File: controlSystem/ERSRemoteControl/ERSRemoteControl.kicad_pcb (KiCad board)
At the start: 2 copper layers, 58.8 x 37.7 mm, 58 parts, among them J1 USB_C_Receptacle_USB2.0_14P, J2 0022-232041, J5 0022-232021, J6 0022-232021, J7 0022-232031, SW2 SW_Push, SW3 SW_Push, SW4 SW_Push, SW5 SW_Push, SW6 SW_Push, SW7 SW_Push, U1 TPS63070, U2 ESP32-S3-WROOM-1

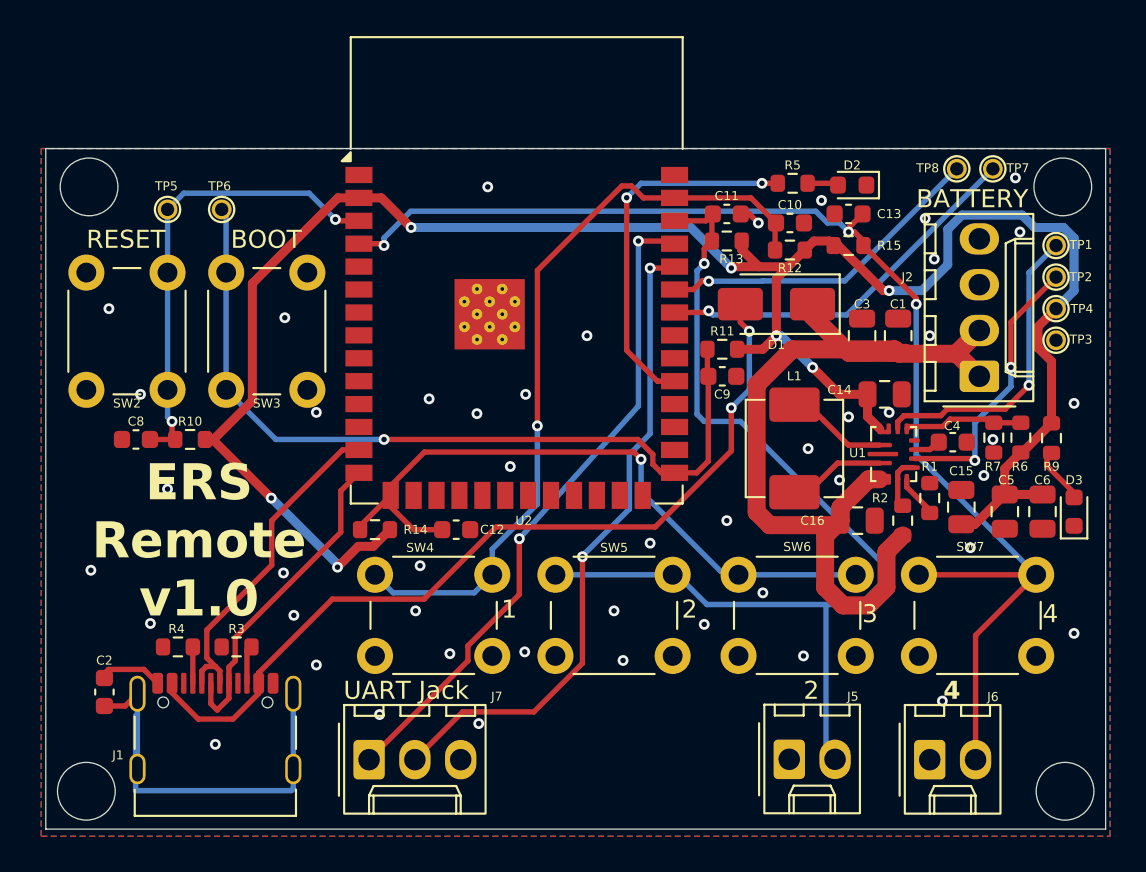
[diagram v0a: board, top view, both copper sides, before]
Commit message: Design review, set board constraints to osh park two layer, fix library paths, etc
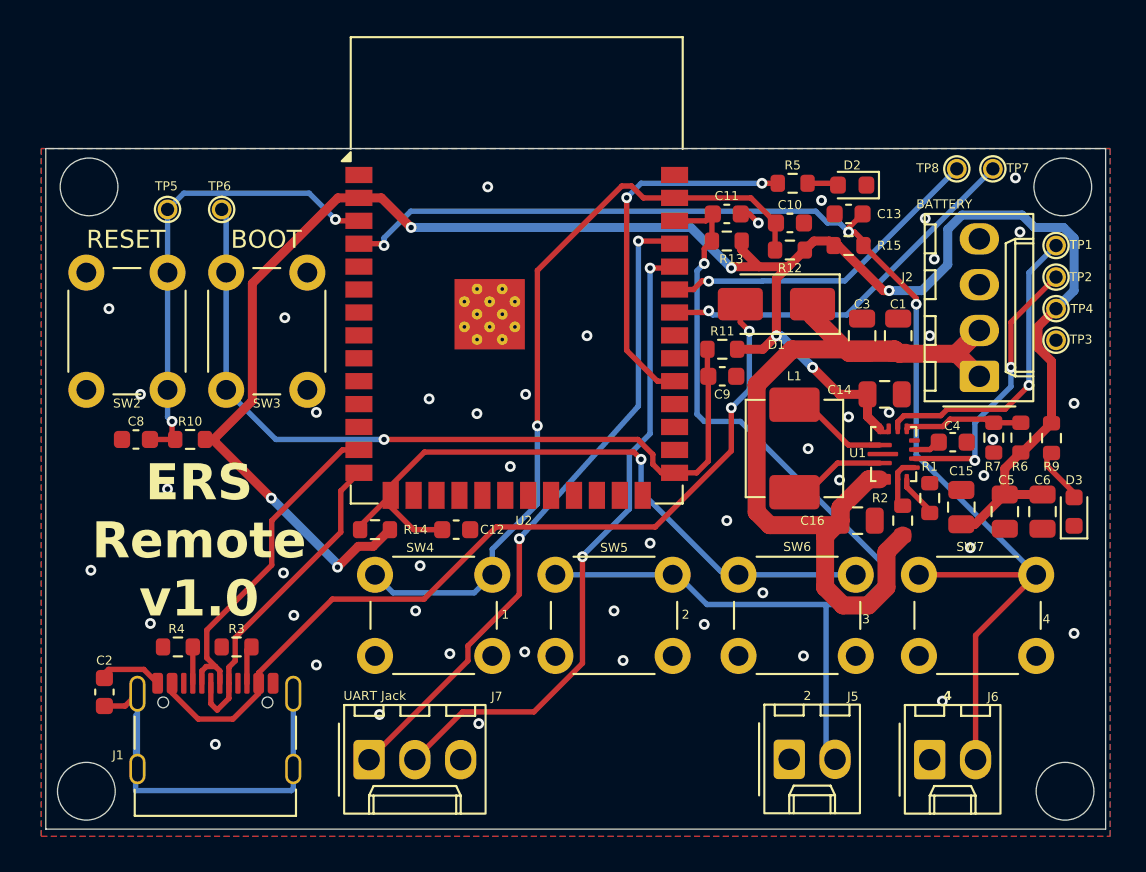
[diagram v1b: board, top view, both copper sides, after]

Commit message: Fixed library issues and completed design review changes
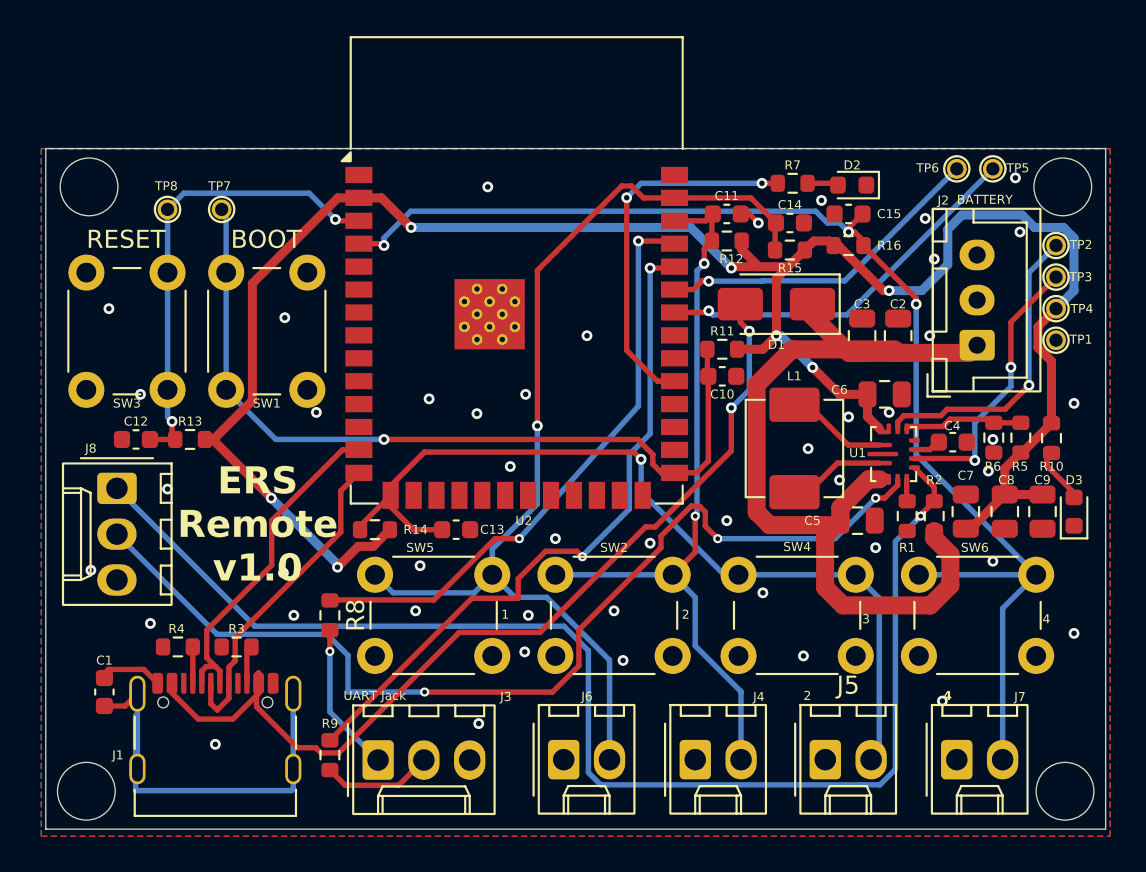
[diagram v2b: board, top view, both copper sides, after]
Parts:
- added J5: 0022-232021, Connector_Molex:Molex_KK-254_AE-6410-02A_1x02_P2.54mm_Vertical, F.Cu at (117.2, 124.8)
- added J6: 0022-232021, Connector_Molex:Molex_KK-254_AE-6410-02A_1x02_P2.54mm_Vertical, F.Cu at (102.7, 124.8)
- added J8: 0022-232031, Connector_Molex:Molex_KK-254_AE-6410-03A_1x03_P2.54mm_Vertical, F.Cu at (77.9, 109.7)
- added R8: 100, Resistor_SMD:R_0603_1608Metric, F.Cu at (89.8, 116.8)
- added R9: 100, Resistor_SMD:R_0603_1608Metric, F.Cu at (89.8, 124.5)
- J2: value 0022-232041 -> B3B-XH-A; footprint Connector_Molex:Molex_KK-254_AE-6410-04A_1x04_P2.54mm_Vertical -> Connector_JST:JST_XH_B3B-XH-A_1x03_P2.50mm_Vertical
- moved J4 5.21 mm to (110.0, 124.8)
- moved R2 1.77 mm to (123.2, 111.2), turned to -90 degrees
- moved J2 1.73 mm to (125.6, 101.8)
- moved R1 1.60 mm to (121.8, 111.2), turned to -90 degrees
- moved J7 1.50 mm to (124.5, 124.8)
- moved J3 0.50 mm to (92.4, 124.8)
- moved C7 0.35 mm to (125.0, 111.0)
- renumbered C2 to C1, C9 to C10, C8 to C12, C12 to C13, C10 to C14, C13 to C15, C1 to C2, C16 to C5, C14 to C6, C15 to C7, C5 to C8, C6 to C9, J7 to J3, J5 to J4, J6 to J7, R9 to R10, R13 to R12, R10 to R13, R12 to R15, R15 to R16, R6 to R5, R7 to R6, R5 to R7, SW3 to SW1, SW5 to SW2, SW2 to SW3, SW6 to SW4, SW4 to SW5, SW7 to SW6, TP3 to TP1, TP1 to TP2, TP2 to TP3, TP7 to TP5, TP8 to TP6, TP6 to TP7, TP5 to TP8
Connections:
- J2 pad 2: Net-(D1-K) -> unconnected-(J2-Pin_2-Pad2)
- J3 pad 1: Net-(J7-Pin_1) -> Net-(J3-Pin_1)
- J3 pad 2: Net-(J7-Pin_2) -> Net-(J3-Pin_2)
- R2 pad 1: Net-(D1-K) -> Net-(J8-Pin_1)
- R2 pad 2: Net-(U1-EN) -> Net-(D1-K)
- U1 pad 1: Net-(U1-EN) -> Net-(J8-Pin_1)
- U1 pad 14: Net-(U1-EN) -> Net-(J8-Pin_2)
- U2 pad 36: Net-(J7-Pin_2) -> Net-(U2-RXD0)
- U2 pad 37: Net-(J7-Pin_1) -> Net-(U2-TXD0)
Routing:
- net Net-(J8-Pin_1): track 0.00 -> 72.3 mm, vias 0 -> 1
- net Net-(J8-Pin_2): track 0.00 -> 56.7 mm, vias 0 -> 3
- net Net-(U2-RXD0): track 0.00 -> 38.0 mm, vias 0 -> 2
- net Net-(J7-Pin_1): track 36.8 -> 0.00 mm, vias 2 -> 0
- net Net-(J7-Pin_2): track 36.4 -> 0.00 mm, vias 2 -> 0
- net Net-(U2-TXD0): track 0.00 -> 33.0 mm, vias 0 -> 2
- net /SWITCH 2: track 56.9 -> 41.8 mm, vias 1 -> 2
- net /SWITCH 1: track 42.8 -> 56.7 mm
- net /SWITCH 3: track 37.6 -> 48.5 mm
- net Net-(J3-Pin_1): track 0.00 -> 8.30 mm, vias 0 -> 1
- net Net-(J3-Pin_2): track 0.00 -> 6.14 mm
- net +5V: track 47.7 -> 52.7 mm
- net Net-(U1-EN): track 3.00 -> 0.00 mm
- net Net-(U1-VSEL): track 2.39 -> 1.23 mm
- net Net-(D1-K): track 49.1 -> 50.2 mm
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
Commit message: Made the traces prettier but still not pretty
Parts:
- moved R8 4.25 mm to (89.8, 121.0)
- moved J2 0.22 mm to (125.6, 102.0)
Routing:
- net Net-(J8-Pin_1): track 72.3 -> 53.1 mm
- net +5V: track 52.7 -> 47.9 mm, vias 2 -> 4
- net /SWITCH 3: track 48.5 -> 44.1 mm, vias 1 -> 2
- net Net-(J3-Pin_1): track 8.30 -> 4.05 mm
- net /SWITCH 1: track 56.7 -> 54.0 mm
- net Net-(U2-TXD0): track 33.0 -> 35.3 mm
- net Net-(U2-RXD0): track 38.0 -> 36.1 mm
- net GND: track 6.36 -> 5.17 mm, vias 46 -> 45
- net Net-(J8-Pin_2): track 56.7 -> 55.5 mm, vias 3 -> 1
- net +3.3V: track 116.9 -> 116.0 mm
- net /SWITCH 2: vias 2 -> 1
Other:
- board text added: "POWER SWITCH"

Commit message: Final trace tweaks and checking voltages
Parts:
- renumbered C5 to C4, C4 to C5, J8 to J3, J3 to J4, J4 to J5, J5 to J6, J6 to J7, J7 to J8, R2 to R1, R1 to R2
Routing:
- net Net-(J3-Pin_2): track 55.5 -> 51.4 mm

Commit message: My name and version number added
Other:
- board text added: "ERS Remote"
- board text added: "Thomas C. Santhosh"
- board text added: "v1.0 9/6/2026"
- board text removed: "ERS Remote v1.0"
